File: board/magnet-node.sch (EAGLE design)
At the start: 32 parts, among them IC1 MSP430G2X21, IC2 HTU21D, IC3 SI4012

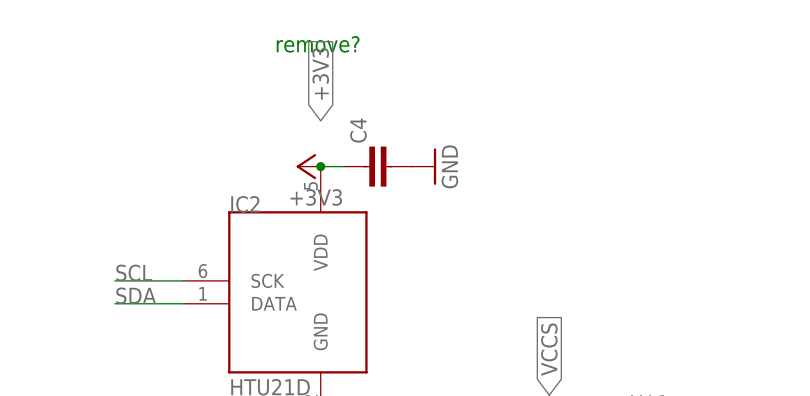
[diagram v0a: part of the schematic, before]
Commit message: adding stencil and couple of values
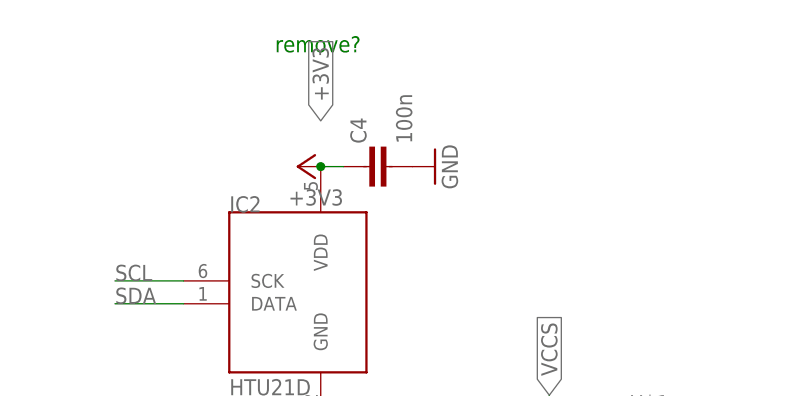
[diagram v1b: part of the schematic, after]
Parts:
- C4: value (none) -> 100n
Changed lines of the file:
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@@
 <part name="IC2" library="Mine" deviceset="HTU21D" device=""/>
 <part name="GND17" library="supply1" deviceset="GND" device=""/>
-<part name="C4" library="passives-7351" deviceset="CAPACITOR" device="0603-N"/>
+<part name="C4" library="passives-7351" deviceset="CAPACITOR" device="0603-N" value="100n"/>
 <part name="GND18" library="supply1" deviceset="GND" device=""/>
 <part name="R4" library="passives-7351" deviceset="RESISTOR" device="0603-N" value="4k7"/>

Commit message: fixing value
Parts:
- C10: value 47n -> 2n2
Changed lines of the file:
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@@
 <part name="GND15" library="supply1" deviceset="GND" device=""/>
 <part name="R3" library="passives-7351" deviceset="RESISTOR" device="0603-N" value="22k"/>
-<part name="C10" library="passives-7351" deviceset="CAPACITOR" device="0603-N" value="47n"/>
+<part name="C10" library="passives-7351" deviceset="CAPACITOR" device="0603-N" value="2n2"/>
 <part name="GND16" library="supply1" deviceset="GND" device=""/>
 <part name="+3V8" library="supply1" deviceset="+3V3" device=""/>
